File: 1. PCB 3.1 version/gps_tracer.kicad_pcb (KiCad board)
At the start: 2 copper layers, 65 x 38.2 mm, 93 parts, among them IC1 TC4056A, J1 Mic, J2 SPK, J3 I2C, J4 BATTERY, J5 Micro_SD_Card, P1 USB_C_Plug_USB2.0, Q1 S8050, Q2 S8050, Q3 FDN358P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

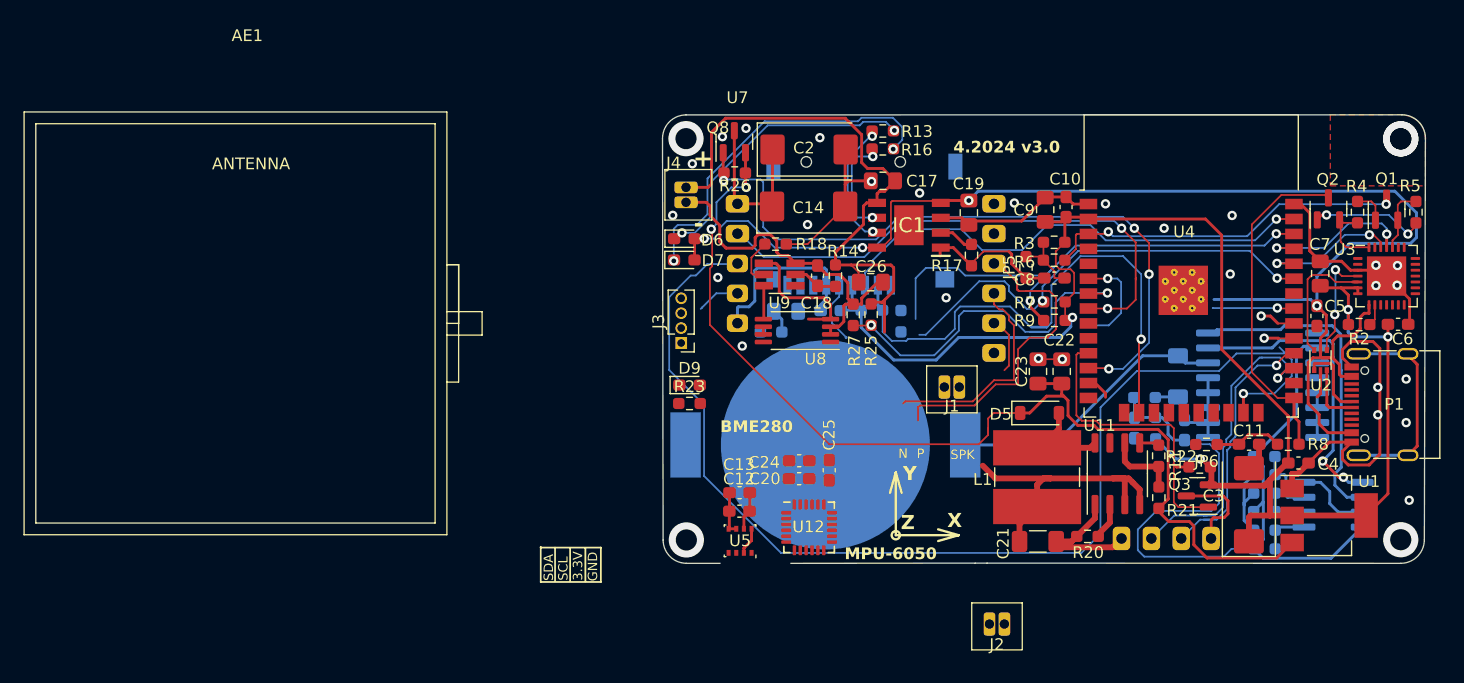
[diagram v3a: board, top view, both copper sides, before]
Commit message: HTTP file server added into /Parts project/6. Web server/13. HTTP file server. The files in Micro SD card can be deleted or download from browser
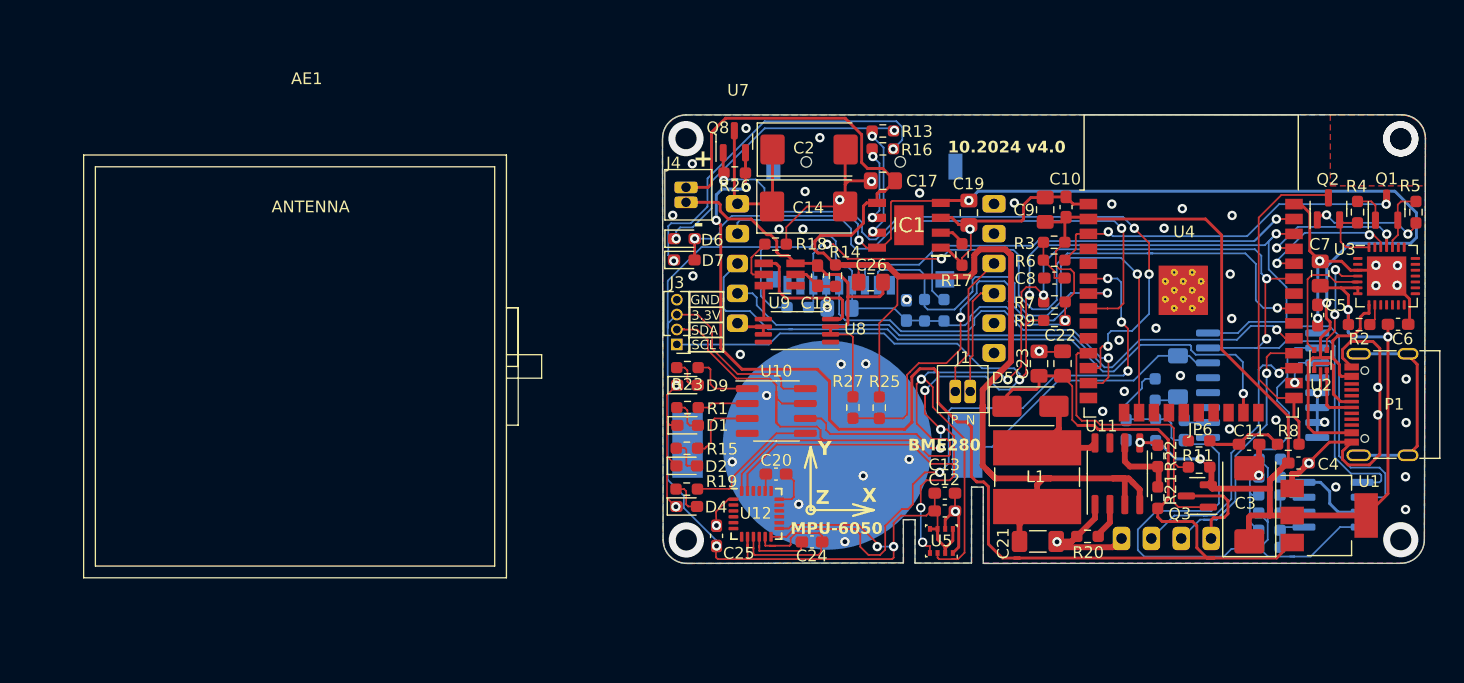
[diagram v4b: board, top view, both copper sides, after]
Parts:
- removed J2: SPK, Footprint_library:JST 1.25
- removed JP5: EN, Resistor_SMD:R_0603_1608Metric_Pad0.98x0.95mm_HandSolder
- added D1: GREEN LED, LED_SMD:LED_0603_1608Metric_Pad1.05x0.95mm_HandSolder, F.Cu at (50.4, 63.4)
- added D2: BLUE LED, LED_SMD:LED_0603_1608Metric_Pad1.05x0.95mm_HandSolder, F.Cu at (50.3, 66.9)
- added D4: YELLOW_LED, LED_SMD:LED_0603_1608Metric_Pad1.05x0.95mm_HandSolder, F.Cu at (50.3, 70.3)
- added R1: 700, Resistor_SMD:R_0603_1608Metric_Pad0.98x0.95mm_HandSolder, F.Cu at (50.4, 61.9)
- added R15: 700, Resistor_SMD:R_0603_1608Metric_Pad0.98x0.95mm_HandSolder, F.Cu at (50.3, 65.4)
- added R19: 700, Resistor_SMD:R_0603_1608Metric_Pad0.98x0.95mm_HandSolder, F.Cu at (50.3, 68.9)
- added U10: PCA9536D, Package_SO:SOIC-8_3.9x4.9mm_P1.27mm, F.Cu at (57.9, 62.2)
- D5: value BAT48ZFILM -> SS14; footprint Diode_SMD:D_SOD-123 -> Diode_SMD:D_SMA
- D9: value LED -> RED LED
- moved C12 17.5 mm to (72.3, 70.7)
- moved C13 17.5 mm to (72.3, 69.2)
- moved U5 17.1 mm to (72.0, 73.3)
- moved C25 11.1 mm to (52.8, 72.9)
- moved R25 7.96 mm to (66.7, 61.9)
- moved R27 7.90 mm to (64.5, 61.9)
- moved C24 7.00 mm to (61.0, 73.4), turned to 180 degrees
- moved C16 6.44 mm to (69.0, 53.7), turned to 90 degrees
- moved AE1 6.26 mm to (17.9, 34.4)
- moved U12 4.63 mm to (56.2, 71.0)
- moved C1 4.56 mm to (63.3, 53.5), turned to 180 degrees
- moved R24 4.48 mm to (70.5, 53.6), turned to -90 degrees
- moved R10 3.79 mm to (72.2, 53.6)
- moved R12 3.09 mm to (59.8, 53.4), turned to 180 degrees
- moved R23 3.06 mm to (50.4, 58.5), turned to 180 degrees
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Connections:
- C8 pad 1: Net-(JP5-B) -> GND
- J3 pad 1: SDA -> SCL
- J3 pad 2: SCL -> SDA
- R23 pad 1: RED_LED -> Net-(U10-IO0)
- R3 pad 2: Net-(JP5-B) -> GND
- R6 pad 2: Net-(JP5-B) -> GND
- U4 pad 26: unconnected-(U4-IO4-Pad26) -> EXTERNAL_WOKE_UP
- U4 pad 30: RED_LED -> unconnected-(U4-IO18-Pad30)
- U7 pad 6: Net-(J2-Pin_1) -> unconnected-(U7-SPKM-Pad6)
- U7 pad 7: Net-(J2-Pin_2) -> unconnected-(U7-SPKN-Pad7)
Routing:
- net SCL: track 71.2 -> 171.4 mm, vias 2 -> 8
- net +3.3V: track 148.4 -> 244.3 mm, vias 4 -> 7
- net SDA: track 64.3 -> 153.6 mm, vias 4 -> 5
- net Net-(IC1-BAT): track 75.9 -> 141.6 mm
- net MICROSD_MISO: track 6.94 -> 59.4 mm, vias 1 -> 3
- net MPU5060_INT: track 8.41 -> 57.2 mm, vias 1 -> 4
- net TXD_GSM: track 6.27 -> 52.3 mm
- net RXD_GSM: track 98.4 -> 57.3 mm
- net GSM_POWER_SOURSE: track 89.4 -> 128.9 mm
- net GND: track 149.1 -> 179.7 mm, vias 27 -> 61
- net MICROSD_CLK: track 7.32 -> 32.2 mm, vias 0 -> 1
- net Net-(J1-Pin_2): track 29.2 -> 12.6 mm
- net Net-(U10-IO3): track 0.00 -> 11.6 mm
- net Net-(J1-Pin_1): track 18.5 -> 9.86 mm
- net MICROSD_CS: track 53.9 -> 46.5 mm
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- added copper zone on B.Cu, net GND
- added copper zone on F.Cu, net GND
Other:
- outline, holes or cut-outs redrawn
- board text added: "10.2024 v4.0"
- board text added: "I2C"
- board text removed: "4.2024 v3.0"
- board text removed: "SPK"
